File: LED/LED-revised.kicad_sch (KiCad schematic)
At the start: 4 parts

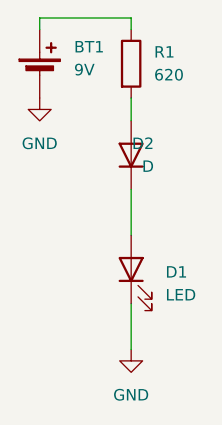
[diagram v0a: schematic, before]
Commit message: Rebuild with real KiCad 9 libraries; verified by kicad-cli ERC/DRC
KiCad is now installed on this host, so the generated project was validated
against KiCad itself rather than only the kicad-happy Python tooling. That
validation found real defects in what had been delivered:

pc-volume-controller.kicad_sch
* now embeds the actual MCU_Module:Arduino_Nano_v3.x, Device:R_Potentiometer,
  Device:C, power:* and Mechanical:MountingHole definitions instead of
  hand-authored symbols (fixes 37 lib_symbol_mismatch warnings)
* every coordinate snapped to the 1.27 mm grid (fixes 70 endpoint_off_grid)
* real library footprints assigned, replacing the invented 'pvc:' namespace
* ERC: 125 violations -> 0

The Nano pinout is now verified rather than assumed: the official symbol
confirms A0-A4 = pins 19-23, +5V = pin 27, GND = pins 4 and 29.

pc-volume-controller.kicad_pcb
* rebuilt from the real Module:Arduino_Nano, Potentiometer_THT and
  Capacitor_SMD footprints with all pads netted
* board fully routed on 2 layers (B.Cu horizontals, F.Cu verticals)
* DRC: 89 violations -> 0, with 0 unconnected items and 0 schematic-parity
  differences

LED/LED-revised.kicad_sch
* added the PWR_FLAG the GND net needs (the battery's negative pin is passive,
  so ERC reported power_pin_not_driven)
* ERC: 1 error -> 0

Validation notes: kicad-cli 9.0.2. Notable format findings - a .kicad_pcb may
not carry a top-level (uuid ...) node (KiCad refuses the board), gr_line stroke
type must be the bare atom 'solid' not a quoted string, and an embedded symbol
must keep leading atoms on its opening line.
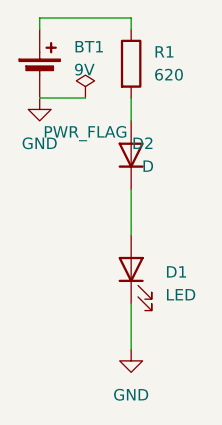
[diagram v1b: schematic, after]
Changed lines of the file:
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@@
+		)
+	)
+	(wire
+		(pts
+			(xy 121.92 57.15)
+			(xy 127 57.15)
+		)
+		(stroke
+			(width 0)
+			(type default)
+		)
+	)
+	(symbol
+		(lib_id "power:PWR_FLAG")
+		(at 127 57.15 0)
+		(unit 1)
+		(exclude_from_sim no)
+		(in_bom yes)
+		(on_board yes)
+		(dnp no)
+		(fields_autoplaced yes)
+		(property "Reference" "#FLG01"
+			(at 127 54.61 0)
+			(effects
+				(font
+					(size 1.27 1.27)
+				)
+				(hide yes)
+			)
+		)
+		(property "Value" "PWR_FLAG"
+			(at 127 60.96 0)
+			(effects
+				(font
+					(size 1.27 1.27)
+				)
+			)
+		)
+		(property "Footprint" ""
+			(at 127 57.15 0)
+			(effects
+				(font
+					(size 1.27 1.27)
+				)
+				(hide yes)
+			)
+		)
+		(property "Datasheet" ""
+			(at 127 57.15 0)
+			(effects
+				(font
+					(size 1.27 1.27)
+				)
+				(hide yes)
+			)
+		)
+		(property "Description" "Special symbol for telling ERC where power comes from"
+			(at 127 57.15 0)
+			(effects
+				(font
+					(size 1.27 1.27)
+				)
+				(hide yes)
+			)
+		)
+		(pin "1"
+		)
+		(instances
+			(project ""
+				(path "/1871d796-7bb9-43f9-8079-125c20ef5a39"
+					(reference "#FLG01")
+					(unit 1)
+				)
+			)
 		)
 	)
